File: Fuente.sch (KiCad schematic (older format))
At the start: 14 parts, among them J5 TB_1X2, P2 USB_OTG, U2 LM2576HVS-5, U3 NCP1117ST33T3G

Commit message: Modificaciones en el schematic dado los componentes comprados empiezo a ordenar los componentes en una dimension estimada de 10x6 cm.
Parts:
- C6: footprint Capacitors_ThroughHole:C_Radial_D13_L21_P5 -> Capacitors_ThroughHole:C_Radial_D10_L25_P5
- C7: footprint Capacitors_ThroughHole:C_Radial_D10_L20_P5 -> Capacitors_ThroughHole:C_Radial_D10_L25_P5
- C8: footprint Capacitors_ThroughHole:C_Radial_D10_L25_P5 -> Capacitors_ThroughHole:C_Radial_D5_L6_P2.5
- D1, D2, D3: footprint Diodes_SMD:SOD-123 -> Diodes_SMD:MELF_Handsoldering
- D4: footprint LEDs:LED_1206 -> Diodes_SMD:MELF_Handsoldering
- J5: footprint Connect:bornier2 -> Connect:AK300-2
- U3: footprint TO_SOT_Packages_SMD:SOT-323 -> TO_SOT_Packages_SMD:TO-252-2Lead
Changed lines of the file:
@@
 F 0 "U3" H 7600 3454 40  0000 C CNN
 F 1 "NCP1117ST33T3G" H 7450 3850 40  0000 C CNN
-F 2 "TO_SOT_Packages_SMD:SOT-323" H 7450 3650 60  0001 C CNN
+F 2 "TO_SOT_Packages_SMD:TO-252-2Lead" H 7450 3650 60  0001 C CNN
 F 3 "~" H 7450 3650 60  0000 C CNN
 	1    7450 3650
@@
 F 0 "C6" H 3950 3600 40  0000 L CNN
 F 1 "470uF" H 3950 3400 40  0000 L CNN
-F 2 "Capacitors_ThroughHole:C_Radial_D13_L21_P5" H 4000 3350 30  0001 C CNN
+F 2 "Capacitors_ThroughHole:C_Radial_D10_L25_P5" H 4000 3350 30  0001 C CNN
 F 3 "~" H 3900 3500 300 0000 C CNN
 	1    3900 3500
@@
 $EndComp
 $Comp
-L GND-RESCUE-ciaa-nxp #PWR011
+L GND-RESCUE-ciaa-nxp #PWR013
 U 1 1 581A2897
 P 3500 3700
-F 0 "#PWR011" H 3500 3700 30  0001 C CNN
+F 0 "#PWR013" H 3500 3700 30  0001 C CNN
 F 1 "GND" H 3500 3630 30  0001 C CNN
 F 2 "" H 3500 3700 60  0000 C CNN
@@
 $EndComp
 $Comp
-L GND-RESCUE-ciaa-nxp #PWR012
+L GND-RESCUE-ciaa-nxp #PWR014
 U 1 1 581A2898
 P 3900 3750
-F 0 "#PWR012" H 3900 3750 30  0001 C CNN
+F 0 "#PWR014" H 3900 3750 30  0001 C CNN
 F 1 "GND" H 3900 3680 30  0001 C CNN
 F 2 "" H 3900 3750 60  0000 C CNN
@@
 $EndComp
 $Comp
-L GND-RESCUE-ciaa-nxp #PWR013
+L GND-RESCUE-ciaa-nxp #PWR015
 U 1 1 581A2899
 P 5000 4050
-F 0 "#PWR013" H 5000 4050 30  0001 C CNN
+F 0 "#PWR015" H 5000 4050 30  0001 C CNN
 F 1 "GND" H 5000 3980 30  0001 C CNN
 F 2 "" H 5000 4050 60  0000 C CNN
@@
 F 0 "D1" H 3500 3350 40  0000 C CNN
 F 1 "MURS360T3G" H 3500 3150 40  0000 C CNN
-F 2 "Diodes_SMD:SOD-123" H 3500 3250 60  0001 C CNN
+F 2 "Diodes_SMD:MELF_Handsoldering" H 3500 3250 60  0001 C CNN
 F 3 "~" H 3500 3250 60  0000 C CNN
 	1    3500 3250
@@
 F 0 "D2" H 5600 4150 40  0000 C CNN
 F 1 "1N5822" H 5600 3950 40  0000 C CNN
-F 2 "Diodes_SMD:SOD-123" H 5600 4050 60  0001 C CNN
+F 2 "Diodes_SMD:MELF_Handsoldering" H 5600 4050 60  0001 C CNN
 F 3 "~" H 5600 4050 60  0000 C CNN
 	1    5600 4050
@@
 $EndComp
 $Comp
-L GND-RESCUE-ciaa-nxp #PWR014
+L GND-RESCUE-ciaa-nxp #PWR016
 U 1 1 581A289D
 P 5600 4300
-F 0 "#PWR014" H 5600 4300 30  0001 C CNN
+F 0 "#PWR016" H 5600 4300 30  0001 C CNN
 F 1 "GND" H 5600 4230 30  0001 C CNN
 F 2 "" H 5600 4300 60  0000 C CNN
@@
 F 0 "C7" H 6650 3950 40  0000 L CNN
 F 1 "1000uF" H 6600 3750 40  0000 L CNN
-F 2 "Capacitors_ThroughHole:C_Radial_D10_L20_P5" H 6700 3700 30  0001 C CNN
+F 2 "Capacitors_ThroughHole:C_Radial_D10_L25_P5" H 6700 3700 30  0001 C CNN
 F 3 "~" H 6600 3850 300 0000 C CNN
 	1    6600 3850
@@
 $EndComp
 $Comp
-L GND-RESCUE-ciaa-nxp #PWR015
+L GND-RESCUE-ciaa-nxp #PWR017
 U 1 1 581A289F
 P 6600 4100
-F 0 "#PWR015" H 6600 4100 30  0001 C CNN
+F 0 "#PWR017" H 6600 4100 30  0001 C CNN
 F 1 "GND" H 6600 4030 30  0001 C CNN
 F 2 "" H 6600 4100 60  0000 C CNN
@@
 $EndComp
 $Comp
-L GND-RESCUE-ciaa-nxp #PWR016
+L GND-RESCUE-ciaa-nxp #PWR018
 U 1 1 581A28A0
 P 7450 4150
-F 0 "#PWR016" H 7450 4150 30  0001 C CNN
+F 0 "#PWR018" H 7450 4150 30  0001 C CNN
 F 1 "GND" H 7450 4080 30  0001 C CNN
 F 2 "" H 7450 4150 60  0000 C CNN
@@
 F 0 "C8" H 8100 3950 40  0000 L CNN
 F 1 "10uF" H 8100 3750 40  0000 L CNN
-F 2 "Capacitors_ThroughHole:C_Radial_D10_L25_P5" H 8150 3700 30  0001 C CNN
+F 2 "Capacitors_ThroughHole:C_Radial_D5_L6_P2.5" H 8150 3700 30  0001 C CNN
 F 3 "~" H 8050 3850 300 0000 C CNN
 	1    8050 3850
@@
 $EndComp
 $Comp
-L GND-RESCUE-ciaa-nxp #PWR017
+L GND-RESCUE-ciaa-nxp #PWR019
 U 1 1 581A28A2
 P 8050 4100
-F 0 "#PWR017" H 8050 4100 30  0001 C CNN
+F 0 "#PWR019" H 8050 4100 30  0001 C CNN
 F 1 "GND" H 8050 4030 30  0001 C CNN
 F 2 "" H 8050 4100 60  0000 C CNN
@@
 F 0 "D3" H 5950 2800 40  0000 C CNN
 F 1 "PMEG3020EH" H 5950 2600 40  0000 C CNN
-F 2 "Diodes_SMD:SOD-123" H 5950 2700 60  0001 C CNN
+F 2 "Diodes_SMD:MELF_Handsoldering" H 5950 2700 60  0001 C CNN
 F 3 "~" H 5950 2700 60  0000 C CNN
 	1    5950 2700
@@
 F 0 "D4" H 6900 4550 50  0000 C CNN
 F 1 "LED red" H 6900 4350 50  0000 C CNN
-F 2 "LEDs:LED_1206" H 6900 4450 60  0001 C CNN
+F 2 "Diodes_SMD:MELF_Handsoldering" H 6900 4450 60  0001 C CNN
 F 3 "~" H 6900 4450 60  0001 C CNN
 	1    6900 4450
@@
 $EndComp
 $Comp
-L GND-RESCUE-ciaa-nxp #PWR018
+L GND-RESCUE-ciaa-nxp #PWR020
 U 1 1 581A28A9
 P 6900 4800
-F 0 "#PWR018" H 6900 4800 30  0001 C CNN
+F 0 "#PWR020" H 6900 4800 30  0001 C CNN
 F 1 "GND" H 6900 4730 30  0001 C CNN
 F 2 "" H 6900 4800 60  0000 C CNN
@@
 $EndComp
 $Comp
-L GND-RESCUE-ciaa-nxp #PWR019
+L GND-RESCUE-ciaa-nxp #PWR021
 U 1 1 581A28AA
 P 6300 4150
-F 0 "#PWR019" H 6300 4150 30  0001 C CNN
+F 0 "#PWR021" H 6300 4150 30  0001 C CNN
 F 1 "GND" H 6300 4080 30  0001 C CNN
 F 2 "" H 6300 4150 60  0000 C CNN
@@
 $EndComp
 $Comp
-L +5V #PWR020
+L +5V #PWR022
 U 1 1 581A28AD
 P 6600 3250
-F 0 "#PWR020" H 6600 3340 20  0001 C CNN
+F 0 "#PWR022" H 6600 3340 20  0001 C CNN
 F 1 "+5V" H 6600 3340 30  0000 C CNN
 F 2 "" H 6600 3250 60  0000 C CNN
@@
 $EndComp
 $Comp
-L +3.3V-RESCUE-ciaa-nxp #PWR021
+L +3.3V-RESCUE-ciaa-nxp #PWR023
 U 1 1 581A28AE
 P 8050 3250
-F 0 "#PWR021" H 8050 3210 30  0001 C CNN
+F 0 "#PWR023" H 8050 3210 30  0001 C CNN
 F 1 "+3.3V" H 8050 3360 30  0000 C CNN
 F 2 "" H 8050 3250 60  0000 C CNN
@@
 $EndComp
 $Comp
-L PWR_FLAG #FLG022
+L PWR_FLAG #FLG024
 U 1 1 581A28B3
 P 6750 3250
-F 0 "#FLG022" H 6750 3345 30  0001 C CNN
+F 0 "#FLG024" H 6750 3345 30  0001 C CNN
 F 1 "PWR_FLAG" H 6750 3430 30  0000 C CNN
 F 2 "" H 6750 3250 60  0000 C CNN
@@
 $EndComp
 $Comp
-L PWR_FLAG #FLG023
+L PWR_FLAG #FLG025
 U 1 1 581A28B7
 P 3350 3700
-F 0 "#FLG023" H 3350 3795 30  0001 C CNN
+F 0 "#FLG025" H 3350 3795 30  0001 C CNN
 F 1 "PWR_FLAG" H 3350 3880 30  0000 C CNN
 F 2 "" H 3350 3700 60  0000 C CNN
@@
 F 0 "J5" H 2750 3600 60  0000 C CNN
 F 1 "TB_1X2" H 2850 3100 60  0000 C CNN
-F 2 "Connect:bornier2" H 2750 3400 60  0001 C CNN
+F 2 "Connect:AK300-2" H 2750 3400 60  0001 C CNN
 F 3 "~" H 2750 3400 60  0000 C CNN
 	1    2800 3350
@@
 $EndComp
 $Comp
-L GND #PWR024
+L GND #PWR026
 U 1 1 581A28BC
 P 4850 2350
-F 0 "#PWR024" H 4850 2100 50  0001 C CNN
+F 0 "#PWR026" H 4850 2100 50  0001 C CNN
 F 1 "GND" H 4850 2200 50  0000 C CNN
 F 2 "" H 4850 2350 50  0000 C CNN
@@
 	6300 3250 5550 3250
 $Comp
-L PWR_FLAG #FLG025
+L PWR_FLAG #FLG027
 U 1 1 581E77AD
 P 3900 3100
-F 0 "#FLG025" H 3900 3195 50  0001 C CNN
+F 0 "#FLG027" H 3900 3195 50  0001 C CNN
 F 1 "PWR_FLAG" H 3900 3280 50  0000 C CNN
 F 2 "" H 3900 3100 50  0000 C CNN

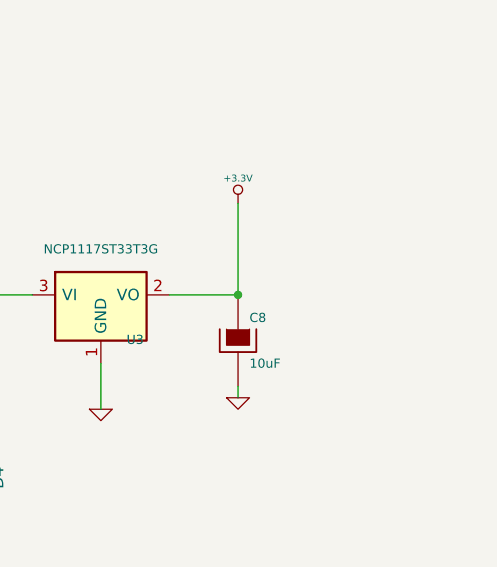
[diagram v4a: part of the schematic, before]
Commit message: Ruteo del PCB, agrego una salida de 5v y 3v en el esquematico
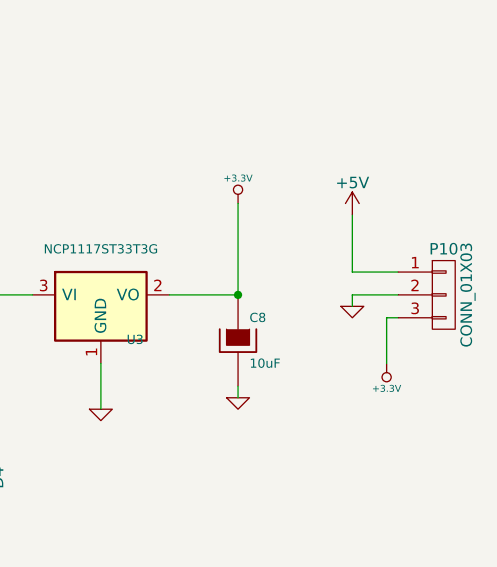
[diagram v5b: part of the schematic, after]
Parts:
- added P10: CONN_01X03, Connect:AK300-3, symbol CONN_01X03
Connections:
- net +3.3V: now also P10.3 (P3)
- net +5V: now also P10.1 (P1)
- net GND: now also P10.2 (P2)
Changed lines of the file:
@@
 	1    0    0    -1
 $EndComp
+$Comp
+L CONN_01X03 P10
+U 1 1 5821D052
+P 8950 3650
+F 0 "P10" H 8950 3850 50  0000 C CNN
+F 1 "CONN_01X03" V 9050 3650 50  0000 C CNN
+F 2 "Connect:AK300-3" H 8950 3650 50  0001 C CNN
+F 3 "" H 8950 3650 50  0000 C CNN
+	1    8950 3650
+	1    0    0    -1
+$EndComp
+Wire Wire Line
+	8550 3550 8750 3550
+Wire Wire Line
+	8550 3300 8550 3550
+$Comp
+L +5V #PWR028
+U 1 1 5821D208
+P 8550 3300
+F 0 "#PWR028" H 8550 3150 50  0001 C CNN
+F 1 "+5V" H 8550 3440 50  0000 C CNN
+F 2 "" H 8550 3300 50  0000 C CNN
+F 3 "" H 8550 3300 50  0000 C CNN
+	1    8550 3300
+	1    0    0    -1
+$EndComp
+$Comp
+L GND-RESCUE-ciaa-nxp #PWR029
+U 1 1 5821D2B8
+P 8550 3700
+F 0 "#PWR029" H 8550 3700 30  0001 C CNN
+F 1 "GND" H 8550 3630 30  0001 C CNN
+F 2 "" H 8550 3700 60  0000 C CNN
+F 3 "" H 8550 3700 60  0000 C CNN
+	1    8550 3700
+	1    0    0    -1
+$EndComp
+Wire Wire Line
+	8750 3650 8550 3650
+Wire Wire Line
+	8550 3650 8550 3700
+Wire Wire Line
+	8750 3750 8700 3750
+Wire Wire Line
+	8700 3750 8700 3950
+$Comp
+L +3.3V-RESCUE-ciaa-nxp #PWR030
+U 1 1 5821D377
+P 8700 3950
+F 0 "#PWR030" H 8700 3910 30  0001 C CNN
+F 1 "+3.3V" H 8700 4060 30  0000 C CNN
+F 2 "" H 8700 3950 60  0000 C CNN
+F 3 "" H 8700 3950 60  0000 C CNN
+	1    8700 3950
+	-1   0    0    1
+$EndComp
 $EndSCHEMATC

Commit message: Change names schematic.
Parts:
- J5: value TB_1X2 -> Vin
- P10: value CONN_01X03 -> 3.3v_GNF_5v
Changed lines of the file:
@@
 P 2800 3350
 F 0 "J5" H 2750 3600 60  0000 C CNN
-F 1 "TB_1X2" H 2850 3100 60  0000 C CNN
+F 1 "Vin" H 2850 3100 60  0000 C CNN
 F 2 "Connect:AK300-2" H 2750 3400 60  0001 C CNN
 F 3 "~" H 2750 3400 60  0000 C CNN
@@
 P 8950 3650
 F 0 "P10" H 8950 3850 50  0000 C CNN
-F 1 "CONN_01X03" V 9050 3650 50  0000 C CNN
+F 1 "3.3v_GNF_5v" V 9050 3650 50  0000 C CNN
 F 2 "Connect:AK300-3" H 8950 3650 50  0001 C CNN
 F 3 "" H 8950 3650 50  0000 C CNN

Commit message: Agrego los graficos para el esquematico en 3d.
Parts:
- D1, D3, D4: footprint Diodes_SMD:MELF_Handsoldering -> Diodes_SMD:MELF_Standard
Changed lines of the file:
@@
 F 0 "D1" H 3500 3350 40  0000 C CNN
 F 1 "MURS360T3G" H 3500 3150 40  0000 C CNN
-F 2 "Diodes_SMD:MELF_Handsoldering" H 3500 3250 60  0001 C CNN
+F 2 "Diodes_SMD:MELF_Standard" H 3500 3250 60  0001 C CNN
 F 3 "~" H 3500 3250 60  0000 C CNN
 	1    3500 3250
@@
 F 0 "D3" H 5950 2800 40  0000 C CNN
 F 1 "PMEG3020EH" H 5950 2600 40  0000 C CNN
-F 2 "Diodes_SMD:MELF_Handsoldering" H 5950 2700 60  0001 C CNN
+F 2 "Diodes_SMD:MELF_Standard" H 5950 2700 60  0001 C CNN
 F 3 "~" H 5950 2700 60  0000 C CNN
 	1    5950 2700
@@
 F 0 "D4" H 6900 4550 50  0000 C CNN
 F 1 "LED red" H 6900 4350 50  0000 C CNN
-F 2 "Diodes_SMD:MELF_Handsoldering" H 6900 4450 60  0001 C CNN
+F 2 "Diodes_SMD:MELF_Standard" H 6900 4450 60  0001 C CNN
 F 3 "~" H 6900 4450 60  0001 C CNN
 	1    6900 4450

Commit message: Add digikey code and comment schematic.
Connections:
- no-connect marks 5 -> 4
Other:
- note added: "Fuente de alimentación con rango aproximado de entrada de 8 a 30V (CC).\nTensiones de salida: 5V, 3A y 3.3V, 1A.\nPosibilidad de alimentar la CIAA a través del puerto USB mediante la conexión con D1."
- note removed: "Fuente de alimentación con rango aproximado de entrada de 12 a 30V (CC).\nTensiones de salida: 5V, 3A y 3.3V, 1A.\nPosibilidad de alimentar la CIAA a través del puerto USB mediante la conexión con D1."
- note removed: "Reemplazo SMD del 1N5825."
- moved on the sheet: C6, C7, C8, D1, D2, D3, D4, J5, L1, P10, P2, R1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
